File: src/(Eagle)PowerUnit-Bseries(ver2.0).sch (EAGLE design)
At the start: 292 parts, among them CON1 XT90PW-M, CON2 XT90PW-F, CON3 XT60PW-F, CON4 XT60PW-F, CON5 XT60PW-F, CON6 XT60PW-F, Q1 SQJA16EP-T1_GE3, Q10 SQJA16EP-T1_GE3, Q11 TMBT3906, Q12 TMBT3906, Q2 SSM3J332R, Q6 SQJA16EP-T1_GE3, SW1 SS-12SDP2, SW2 RDS-16S-1055-SMT-TR, SW3 SSSS213202, SW4 2MS1-T2-B4-M2-Q-E-S, SW5 2MS1-T2-B4-M2-Q-E-S, U1 LQFP64, U10 TC7S14F, U11 MCP6541T-I/LT, U12 MCP6541T-I/LT, U13 TC7S14F, U14 TCK420G, U15 TCKE805NAWSON10B_TOS-REC, U16 TC7SH00FULJ, U17 TC7S14F, U18 TC7S14F, U19 TC7SH00FULJ, U2 MCP2517FD, U20 TLP293, U21 TC7S14F, U22 TC7S14F, U23 TC7S14F, U24 MCP6541T-I/LT, U25 TC7S14F, U26 TC7SH00FULJ, U3 CH340E, U4 CZ-3A04, U5 AP63205WU-7, U6 CZ-3A04, U7 MCP6541T-I/LT, U8 CZ-3A04, U9 CZ-3A04, X1 XRCGB40M000F4M01R0, X2 RH100-24.000-18-1020-EXT-TR, X3 32.768K12.5PI/MC306

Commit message: develop_v2
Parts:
- removed R124: 10, CR0603:CR0603
- removed ZD2: MMBZ5248B-TP, MMBZ5248B-TP:MMBZ5248B-TP
- added LED10, LED9: SML-E12V8WT86, SML-E12V8WT86:SML-E12V8WT86
- added NTC1: NCU15WB473F60RC, NCU15WB473F60RC:NCU15WB473F60RC
- added R79: 680, CR0603:CR0603
- added R80: 33k, CR0603:CR0603
- added R81: 1.8k, CR0603:CR0603
- added R82: 100k, CR0603:CR0603
- added R83: 187k, CR0603:CR0603
- added R84: 0Ω, CR0603:CR0603
- added R85: 100, CR0603:CR0603
- added SB8: RSX101VAM-30TR, RSX101VAM-30TR:RSX101VAM-30TR
- added U27: MCP6541T-I/LT, MCP6541T-I:MCP6541T-I/LT
- R3: value 1 -> 10; device CR0603:CR0603 -> RSMF2JT10R0:RSMF2JT10R0
- R8, R9: value (none) -> 5.1k
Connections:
- removed net GND2: B1.3, C10.P$2, C11.P$2, C12.2, C13.P$1, C14.P$2, C15.P$2, C16.2, C17.2, C18.P$2, C19.P$2, C20.P$2, C21.P$2, C22.P$2, C23.P$2, C24.2, C25.P$2, C26.P$2, C27.1, C28.1, C29.1, C3.P$1, C30.1, C31.P$2, C32.P$2, C33.P$2, C34.P$2, C35.P$2, C36.P$2, C37.P$1, C38.P$1, C39.P$1, C4.R, C40.P$1, C41.P$1, C42.P$1, C43.P$1, C44.2, C45.2, C46.P$1, C47.P$2, C48.2, C49.2, C5.R, C50.P$2, C51.2, C52.2, C53.P$2, C54.2, C55.2, C56.P$2, C57.P$1, C58.P$1, C59.P$1, C60.P$1, C61.P$1, C62.P$1, C63.P$1, C64.P$1, C67.P$2, C68.2, C69.P$2, C7.CATHODE, C8.P$2, C9.2, D3.A, GND.1, JP2.1, JP3.1, JP4.1, JP5.1, JP7.1, LED4.C, LED5.C, LED6.C, LED7.C, ML1.11, ML1.5, ML1.7, POW.1, R100.LEFT, R102.LEFT, R105.LEFT, R107.LEFT, R11.RIGHT, R12.LEFT, R15.LEFT, R19.LEFT, R20.LEFT, R22.RIGHT, R29.LEFT, R30.LEFT, R31.LEFT, R37.LEFT, R38.LEFT, R41.LEFT, R45.RIGHT, R49.LEFT, R54.LEFT, R56.LEFT, R61.RIGHT, R66.RIGHT, R72.RIGHT, R75.LEFT, R76.LEFT, R8.LEFT, R9.LEFT, R95.LEFT, R97.LEFT, RJ45_1.2, RJ45_1.8, RJ45_1.LED2_K, RJ45_2.2, RJ45_2.8, RJ45_2.LED2_K, SB6.A, TLP1.CATHODE, TR1.E, TR2.E, U$1.VSS, U$4.GND, U1.P12, U1.P18, U1.P31, U1.P47, U1.P63, U10.GND, U11.VSS, U12.VSS, U13.GND, U15.GND, U2.VSS, U22.GND, U23.GND, U24.VSS, U25.GND, U26.GND, U3.GND, U4.VSS1, U4.VSS2, U5.GND, U6.VSS1, U6.VSS2, U7.VSS, U8.VSS1, U8.VSS2, U9.VSS1, U9.VSS2, USB1.GND, USB1.SHIELD, X2.SHIELD
- removed net N$112: Q1.G, Q6.G, R124.LEFT, ZD2.C
- new net N$120: LED9.A, R79.RIGHT
- new net N$121: R84.RIGHT, U3.RTS#
- new net N$122: R80.RIGHT, R81.LEFT, R83.LEFT, U27.IN+
- new net N$123: R84.LEFT, U3.CTS#
- new net N$124: LED10.A, R85.RIGHT
- new net N$126: R83.RIGHT, R85.LEFT, SB8.A, U27.OUT
- new net PGND: C1.CATHODE, C2.P$2, C65.P$2, C66.P$2, C70.P$2, C71.P$2, CON1.-, CON2.-, EDGE1.P28, EDGE1.P29, EDGE1.P30, EDGE1.P31, EDGE1.P32, EDGE1.P33, EDGE1.P34, EDGE1.P35, EDGE1.P36, EDGE1.P37, EDGE1.P38, EDGE1.P39, EDGE2.P28, EDGE2.P29, EDGE2.P30, EDGE2.P31, EDGE2.P32, EDGE2.P33, EDGE2.P34, EDGE2.P35, EDGE2.P36, EDGE2.P37, EDGE2.P38, EDGE2.P39, EDGE3.P28, EDGE3.P29, EDGE3.P30, EDGE3.P31, EDGE3.P32, EDGE3.P33, EDGE3.P34, EDGE3.P35, EDGE3.P36, EDGE3.P37, EDGE3.P38, EDGE3.P39, EDGE4.P28, EDGE4.P29, EDGE4.P30, EDGE4.P31, EDGE4.P32, EDGE4.P33, EDGE4.P34, EDGE4.P35, EDGE4.P36, EDGE4.P37, EDGE4.P38, EDGE4.P39, GND.2, H1.P$1, H2.P$1, H3.P$1, H4.P$1, INV_SW2.2, LED1.C, LED2.C, LED9.C, Q10.S, R119.LEFT, SW5.O, TLP1.GND, TLP3.CATHODE, TLP3.GND, U14.GND, U16.GND, U17.GND, U18.GND, U19.GND, U20.EMITTER, U21.GND, ZD1.A, ZD5.A
- new net SGND: B1.3, C10.P$2, C11.P$2, C12.2, C13.P$1, C14.P$2, C15.P$2, C16.2, C17.2, C18.P$2, C19.P$2, C20.P$2, C21.P$2, C22.P$2, C23.P$2, C24.2, C25.P$2, C26.P$2, C27.1, C28.1, C29.1, C3.P$1, C30.1, C31.P$2, C32.P$2, C33.P$2, C34.P$2, C35.P$2, C36.P$2, C37.P$1, C38.P$1, C39.P$1, C4.R, C40.P$1, C41.P$1, C42.P$1, C43.P$1, C44.2, C45.2, C46.P$1, C47.P$2, C48.2, C49.2, C5.R, C50.P$2, C51.2, C52.2, C53.P$2, C54.2, C55.2, C56.P$2, C57.P$1, C58.P$1, C59.P$1, C60.P$1, C61.P$1, C62.P$1, C63.P$1, C64.P$1, C67.P$2, C68.2, C69.P$2, C7.CATHODE, C8.P$2, C9.2, D3.A, GND.1, JP2.1, JP3.1, JP4.1, JP5.1, JP7.1, LED10.C, LED4.C, LED5.C, LED6.C, LED7.C, ML1.11, ML1.5, ML1.7, NTC1.1, POW.1, R100.LEFT, R102.LEFT, R105.LEFT, R107.LEFT, R11.RIGHT, R12.LEFT, R15.LEFT, R19.LEFT, R20.LEFT, R22.RIGHT, R29.LEFT, R30.LEFT, R31.LEFT, R37.LEFT, R38.LEFT, R41.LEFT, R45.RIGHT, R49.LEFT, R54.LEFT, R56.LEFT, R61.RIGHT, R66.RIGHT, R72.RIGHT, R75.LEFT, R76.LEFT, R8.LEFT, R81.RIGHT, R9.LEFT, R95.LEFT, R97.LEFT, RJ45_1.2, RJ45_1.8, RJ45_1.LED2_K, RJ45_2.2, RJ45_2.8, RJ45_2.LED2_K, SB6.A, TLP1.CATHODE, TR1.E, TR2.E, U$1.VSS, U$4.GND, U1.P12, U1.P18, U1.P31, U1.P47, U1.P63, U10.GND, U11.VSS, U12.VSS, U13.GND, U15.GND, U2.VSS, U22.GND, U23.GND, U24.VSS, U25.GND, U26.GND, U27.VSS, U3.GND, U4.VSS1, U4.VSS2, U5.GND, U6.VSS1, U6.VSS2, U7.VSS, U8.VSS1, U8.VSS2, U9.VSS1, U9.VSS2, USB1.GND, USB1.SHIELD, X2.SHIELD
- new net THERMAL: NTC1.2, R82.RIGHT, U1.P21, U27.IN-
- net +3V3: now also R80.LEFT, R82.LEFT, U27.VDD
- net CS1_OCD1: no longer C48.1, C51.1, C54.1, JP1.3, JP10.3, JP9.3, R24.LEFT, R63.LEFT, R69.LEFT
- net CS1_OCD2: no longer C49.1, C52.1, C55.1, JP1.1, JP10.1, JP9.1, R33.LEFT, R64.LEFT, R70.LEFT
- net CS2_OCD1: now also C48.1, JP1.3, R24.LEFT
- net CS2_OCD2: now also C49.1, JP1.1, R33.LEFT
- net CS3_OCD1: now also C51.1, JP9.3, R63.LEFT
- net CS3_OCD2: now also C52.1, JP9.1, R64.LEFT
- net CS4_OCD1: now also C54.1, JP10.3, R69.LEFT
- net CS4_OCD2: now also C55.1, JP10.1, R70.LEFT
- net GND: no longer C1.CATHODE, C2.P$2, C65.P$2, C66.P$2, C70.P$2, C71.P$2, CON1.-, CON2.-, EDGE1.P28, EDGE1.P29, EDGE1.P30, EDGE1.P31, EDGE1.P32, EDGE1.P33, EDGE1.P34, EDGE1.P35, EDGE1.P36, EDGE1.P37, EDGE1.P38, EDGE1.P39, EDGE2.P28, EDGE2.P29, EDGE2.P30, EDGE2.P31, EDGE2.P32, EDGE2.P33, EDGE2.P34, EDGE2.P35, EDGE2.P36, EDGE2.P37, EDGE2.P38, EDGE2.P39, EDGE3.P28, EDGE3.P29, EDGE3.P30, EDGE3.P31, EDGE3.P32, EDGE3.P33, EDGE3.P34, EDGE3.P35, EDGE3.P36, EDGE3.P37, EDGE3.P38, EDGE3.P39, EDGE4.P28, EDGE4.P29, EDGE4.P30, EDGE4.P31, EDGE4.P32, EDGE4.P33, EDGE4.P34, EDGE4.P35, EDGE4.P36, EDGE4.P37, EDGE4.P38, EDGE4.P39, GND.2, H1.P$1, H2.P$1, H3.P$1, H4.P$1, INV_SW2.2, LED1.C, LED2.C, Q10.S, R119.LEFT, SW5.O, TLP1.GND, TLP3.CATHODE, TLP3.GND, U14.GND, U16.GND, U17.GND, U18.GND, U19.GND, U20.EMITTER, U21.GND, ZD1.A, ZD5.A
- net N$11: now also R3.1; no longer R3.RIGHT
- net N$111: now also R3.2; no longer R3.LEFT, ZD2.A
- net N$25: now also C1.ANODE, R79.LEFT
- net N$26: now also Q1.G, Q6.G; no longer R124.RIGHT
- net SHUTDOWN: now also SB8.C
- net VCC: no longer C1.ANODE
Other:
- note added: "A"
- note added: "Default:closed"
- note added: "Default:open"
- note added: "Hysteresis:5℃(approximately)"
- note added: "Near the high-side MOSFETs"
- note added: "OTP"
- note added: "S=GND->normal mode S=VIN->silent mode"
- note removed: "Sピン=GND->通常モード Sピン=VIN->サイレントモード"
- moved on the sheet: B1, C1, C26, C67, C9, CON1, CON2, D3, FUSE1, LED1, R2

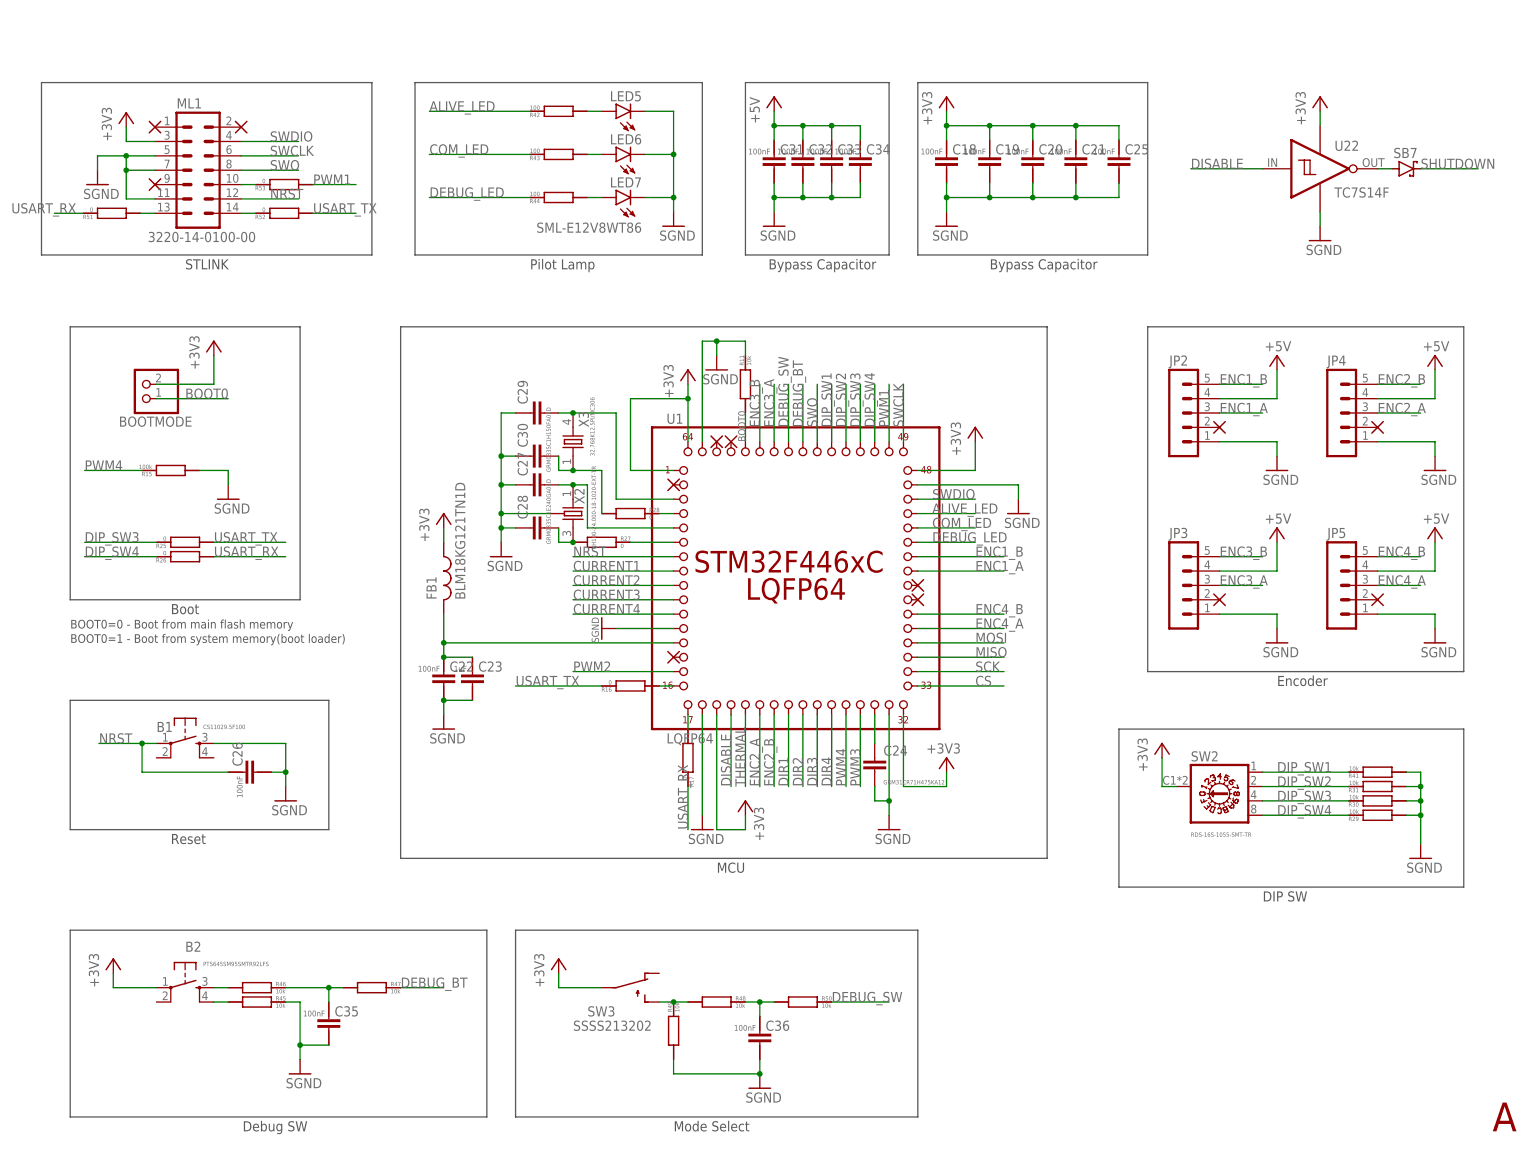
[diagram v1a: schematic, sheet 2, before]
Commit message: 2023/03/07 信号ラインの配線途中
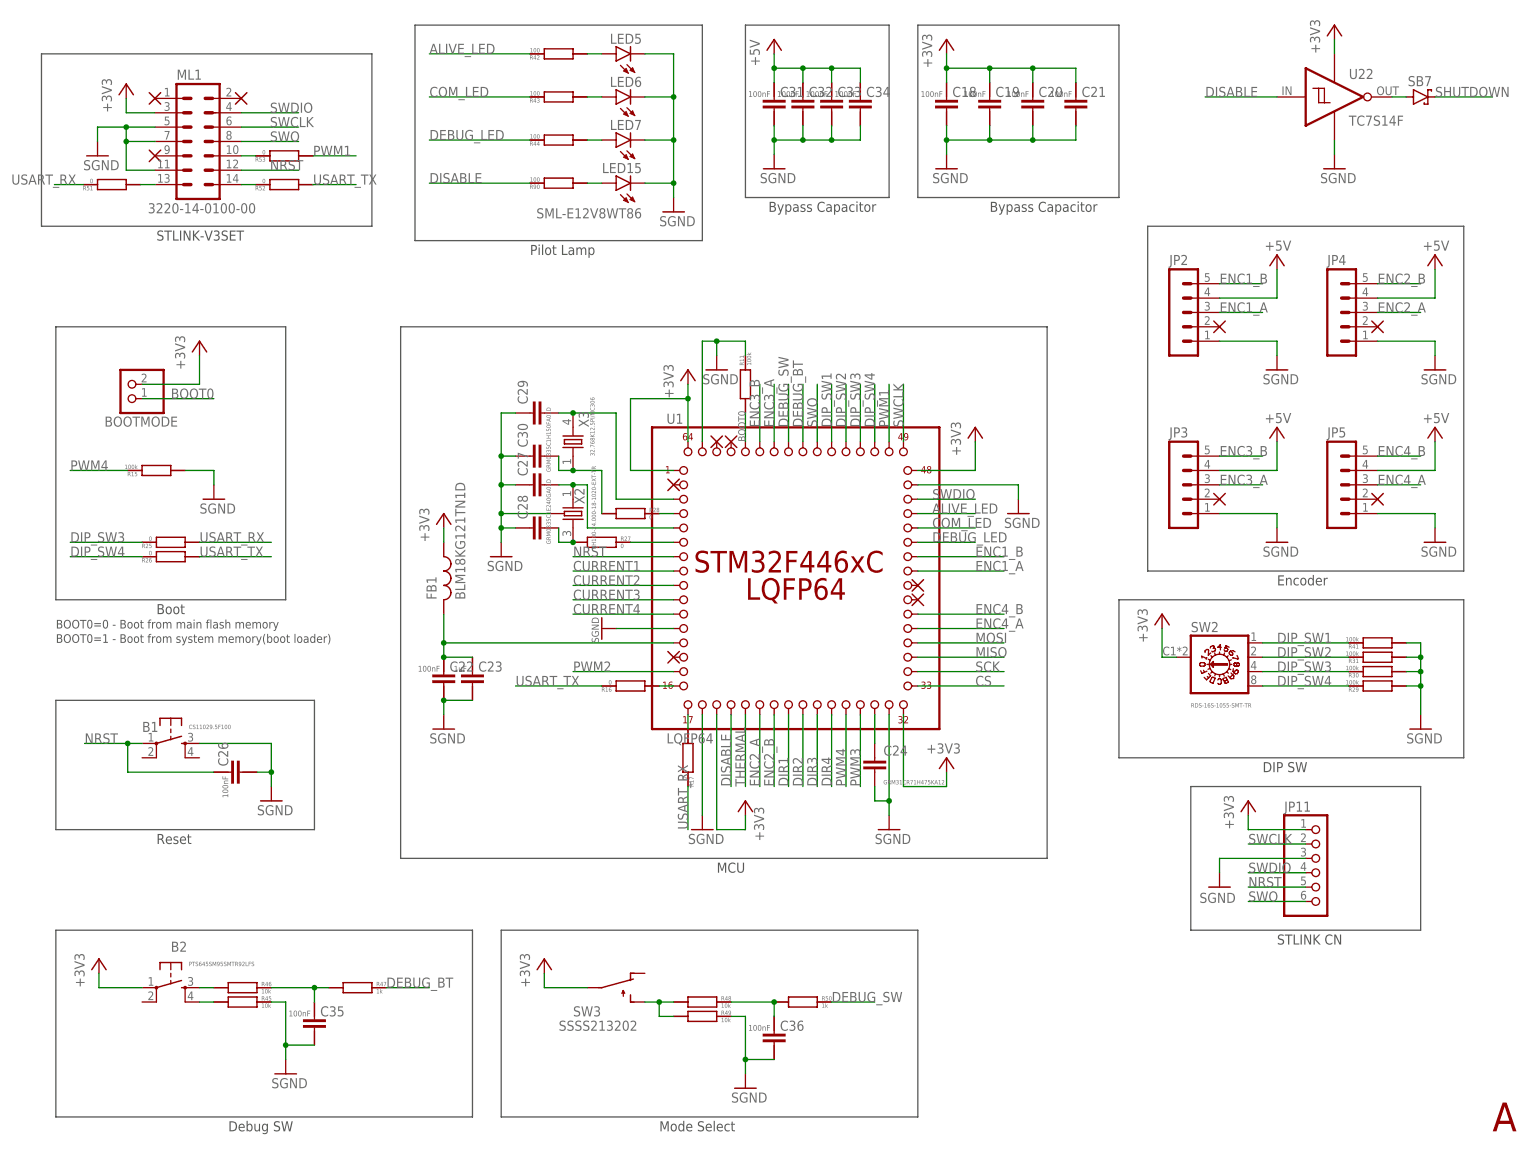
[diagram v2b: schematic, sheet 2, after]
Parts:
- removed C1: 50SEV470M16X16.5, 50SEV470M16X16.5:50SEV470M16X16.5
- removed C25: GCM188L81H104KA57, GCM188L81H104K57(0.1uF):GCM188L81H104KA57
- removed CON6: XT60PW-F, amass:XT60PW-F
- added C72, C73: GCM188L81H104KA57, GCM188L81H104K57(0.1uF):GCM188L81H104KA57
- added D4: GS2M-LTP, GS2M-LTP:GS2M-LTP
- added HEATSINK1: V2020B, V2020B:V2020B
- added IN: XT90PW-M, amass:XT90PW-M
- added JP11: (no value), pinhead:PINHD-1X6
- added LED11, LED12, LED13, LED14, LED15: SML-E12V8WT86, SML-E12V8WT86:SML-E12V8WT86
- added R86, R87, R89: 150, CR0603:CR0603
- added R88, R90: 100, CR0603:CR0603
- C39, C40, C41, C42, C58, C59, C62, C63: value GCM188L81H104KA57 -> GRM1885C1H102JA01D; device GCM188L81H104K57(0.1uF):GCM188L81H104KA57 -> GRM1885C1H102JA01D:GRM1885C1H102JA01D
- CON1: value XT90PW-M -> XT60PW-F; device amass:XT90PW-M -> amass:XT60PW-F
- CON2: value XT90PW-F -> XT60PW-F; device amass:XT90PW-F -> amass:XT60PW-F
- CON5: value XT60PW-F -> XT90PW-F; device amass:XT60PW-F -> amass:XT90PW-F
- D1, D2: value GS1010FL -> GS2M-LTP; device GS1010FL:GS1010FL -> GS2M-LTP:GS2M-LTP
- INV_SW1, INV_SW2: value (none) -> 02-JST; device pinhead:PINHD-1X2 -> con-jst-xh:02-JST
- R11, R29, R30, R31, R41: value 10k -> 100k
- R113, R116, R2, R5, R79: value 680 -> 1.1k
- R120: value 620 -> 1k
- R32: value 10k -> 10
- R4: value 220 -> 560
- R47, R50: value 10k -> 1k
- R76: value 36k -> 56k
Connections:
- removed net GND: EDGE1.P24, EDGE2.P24, EDGE3.P24, EDGE4.P24
- removed net N$15: CTRL1.2, CTRL2.2, R4.LEFT, THRU1.2, THRU2.2
- removed net VCC2: EDGE1.P27, EDGE2.P27, EDGE3.P27, EDGE4.P27
- new net E5V: C7.ANODE, JP6.3, L1.R, R86.RIGHT, U5.FB
- new net N$112: D4.A, R32.LEFT
- new net N$125: LED11.A, R86.LEFT
- new net N$127: LED15.A, R90.LEFT
- new net N$129: LED13.A, R89.LEFT
- new net N$130: LED14.A, R88.LEFT
- net +3V3: now also C72.P$1, EDGE1.P27, EDGE2.P27, EDGE3.P27, EDGE4.P27, JP11.1, R88.RIGHT; no longer C25.P$1
- net +5V: now also R89.RIGHT; no longer R32.RIGHT
- net 5V1: now also C73.P$1
- net CS1_REF1: now also C41.1; no longer C41.P$2
- net CS1_REF2: now also C42.1; no longer C42.P$2
- net CS2_REF1: now also C39.1; no longer C39.P$2
- net CS2_REF2: now also C40.1; no longer C40.P$2
- net CS3_REF1: now also C58.1; no longer C58.P$2
- net CS3_REF2: now also C59.1; no longer C59.P$2
- net CS4_REF1: now also C62.1; no longer C62.P$2
- net CS4_REF2: now also C63.1; no longer C63.P$2
- net DISABLE: now also R90.RIGHT
- net IP1: now also CON1.-; no longer CON3.-
- net IP2: now also CON2.-; no longer CON4.-
- net IP3: now also CON3.-; no longer CON5.-
- net IP4: now also CON4.-; no longer CON6.-
- net N$10: now also CON4.+; no longer CON6.+
- net N$103: no longer R32.LEFT
- net N$25: now also IN.+; no longer C1.ANODE, CON1.+
- net N$4: now also CON1.+; no longer CON3.+
- net N$5: now also CON2.+; no longer CON4.+
- net N$55: now also LED12.A, R87.LEFT; no longer C7.ANODE, JP6.3, L1.R, U5.FB
- net N$6: now also CON3.+; no longer CON5.+
- net N$63: now also R49.LEFT; no longer R49.RIGHT
- net N$95: now also D4.C
- net N$96: now also R32.RIGHT
- net NRST: now also JP11.5
- net PGND: now also C73.P$2, CON5.-, IN.-; no longer C1.CATHODE, CON1.-, CON2.-
- net SGND: now also C39.2, C40.2, C41.2, C42.2, C58.2, C59.2, C62.2, C63.2, C72.P$2, EDGE1.P24, EDGE2.P24, EDGE3.P24, EDGE4.P24, JP11.3, LED11.C, LED12.C, LED13.C, LED14.C, LED15.C, R49.RIGHT; no longer C25.P$2, C39.P$1, C40.P$1, C41.P$1, C42.P$1, C58.P$1, C59.P$1, C62.P$1, C63.P$1, R49.LEFT
- net SWCLK: now also JP11.2
- net SWDIO: now also JP11.4
- net SWO: now also JP11.6
- net U5V: now also R87.RIGHT
- net USART_RX: now also R25.LEFT; no longer R26.LEFT
- net USART_TX: now also R26.LEFT; no longer R25.LEFT
- net VCC: now also CON5.+, CTRL1.2, CTRL2.2, R4.LEFT, THRU1.2, THRU2.2; no longer CON2.+
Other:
- note added: "23.368℃/W"
- note added: "BOOT1"
- note added: "Continuous Max:92[A]"
- note added: "DeadTime:0.606ms(approximately)"
- note added: "RJ45(CH1)"
- note added: "RJ45(CH2)"
- note added: "STLINK CN"
- note added: "STLINK-V3SET"
- note added: "UVLO:5.434V"
- note added: "V_ON:5.883V"
- note added: "limit:1.35A"
- note added: "limit:1.948A"
- note removed: "DeadTime:0.568ms(approximately)"
- note removed: "RJ45"
- note removed: "STLINK"
- note removed: "limit:2.956A"
- moved on the sheet: B1, B2, BOOTMODE, C18, C19, C20, C21, C26, C31, C32, C33, C34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

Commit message: 2023/03/10の進捗
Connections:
- removed net CANH: R7.RIGHT, RJ45_1.3, RJ45_1.4, RJ45_2.3, RJ45_2.4, U$1.CANH
- removed net CANL: RJ45_1.5, RJ45_1.6, RJ45_2.5, RJ45_2.6, SW1.C, U$1.CANL
- new net CAN_H: R7.RIGHT, RJ45_1.5, RJ45_1.6, RJ45_2.5, RJ45_2.6, U$1.CANH
- new net CAN_L: RJ45_1.3, RJ45_1.4, RJ45_2.3, RJ45_2.4, SW1.C, U$1.CANL
- net PGND: no longer H3.P$1, H4.P$1
- net SGND: now also H3.P$1, H4.P$1
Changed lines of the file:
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@@
 <part name="CON5" library="amass" library_urn="urn:adsk.eagle:library:38637493" deviceset="XT90" device="PW-F" package3d_urn="urn:adsk.eagle:package:38637515/3"/>
 <part name="P+25" library="supply1" library_urn="urn:adsk.eagle:library:371" deviceset="VCC" device=""/>
+<part name="GND72" library="supply1" library_urn="urn:adsk.eagle:library:371" deviceset="GND" device=""/>
 </parts>
 <sheets>
@@
 <attribute name="VALUE" x="24.892" y="15.3162" size="1.778" layer="96"/>
 </instance>
-<instance part="SUPPLY4" gate="GND" x="12.7" y="15.24" smashed="yes"/>
+<instance part="SUPPLY4" gate="GND" x="7.62" y="25.4" smashed="yes"/>
 <instance part="USB1" gate="G$1" x="83.82" y="30.48" smashed="yes">
 <attribute name="VALUE" x="73.314" y="64.51" size="2" layer="96"/>
@@
 <attribute name="VALUE" x="66.04" y="297.18" size="1.778" layer="96" rot="R90"/>
 </instance>
+<instance part="GND72" gate="1" x="7.62" y="15.24" smashed="yes"/>
 </instances>
 <busses>
@@
 <pinref part="SUPPLY4" gate="GND" pin="GND"/>
 <pinref part="H1" gate="G$1" pin="P$1"/>
-<wire x1="12.7" y1="17.78" x2="12.7" y2="22.86" width="0.1524" layer="91"/>
-<wire x1="12.7" y1="22.86" x2="12.7" y2="27.94" width="0.1524" layer="91"/>
+<wire x1="7.62" y1="27.94" x2="12.7" y2="27.94" width="0.1524" layer="91"/>
 <wire x1="12.7" y1="27.94" x2="12.7" y2="33.02" width="0.1524" layer="91"/>
 <wire x1="12.7" y1="33.02" x2="22.86" y2="33.02" width="0.1524" layer="91"/>
@@
 <wire x1="22.86" y1="27.94" x2="12.7" y2="27.94" width="0.1524" layer="91"/>
 <junction x="12.7" y="27.94"/>
-<pinref part="H3" gate="G$1" pin="P$1"/>
-<wire x1="22.86" y1="22.86" x2="12.7" y2="22.86" width="0.1524" layer="91"/>
-<junction x="12.7" y="22.86"/>
-<pinref part="H4" gate="G$1" pin="P$1"/>
-<wire x1="22.86" y1="17.78" x2="12.7" y2="17.78" width="0.1524" layer="91"/>
-<junction x="12.7" y="17.78"/>
-<label x="9.652" y="11.176" size="1.778" layer="95"/>
+<label x="4.572" y="21.844" size="1.778" layer="95"/>
 </segment>
 <segment>
@@
 <label x="160.02" y="388.62" size="1.778" layer="95"/>
 </segment>
+<segment>
+<pinref part="H4" gate="G$1" pin="P$1"/>
+<pinref part="GND72" gate="1" pin="GND"/>
+<wire x1="22.86" y1="17.78" x2="12.7" y2="17.78" width="0.1524" layer="91"/>
+<pinref part="H3" gate="G$1" pin="P$1"/>
+<wire x1="12.7" y1="17.78" x2="7.62" y2="17.78" width="0.1524" layer="91"/>
+<wire x1="22.86" y1="22.86" x2="12.7" y2="22.86" width="0.1524" layer="91"/>
+<wire x1="12.7" y1="22.86" x2="12.7" y2="17.78" width="0.1524" layer="91"/>
+<junction x="12.7" y="17.78"/>
+<label x="4.572" y="12.7" size="1.778" layer="95"/>
+</segment>
 </net>
 <net name="THERMAL" class="0">
@@
 </busses>
 <nets>
-<net name="CANH" class="0">
+<net name="CAN_H" class="0">
 <segment>
 <pinref part="U$1" gate="G$1" pin="CANH"/>
@@
 </segment>
 <segment>
-<pinref part="RJ45_1" gate="G$1" pin="4"/>
-<wire x1="81.28" y1="116.84" x2="81.28" y2="109.22" width="0.1524" layer="91"/>
-<label x="81.28" y="109.22" size="1.778" layer="95" rot="R90"/>
+<pinref part="RJ45_1" gate="G$1" pin="5"/>
+<wire x1="83.82" y1="116.84" x2="83.82" y2="109.22" width="0.1524" layer="91"/>
+<label x="83.82" y="109.22" size="1.778" layer="95" rot="R90"/>
 </segment>
 <segment>
-<pinref part="RJ45_1" gate="G$1" pin="3"/>
-<wire x1="78.74" y1="116.84" x2="78.74" y2="109.22" width="0.1524" layer="91"/>
-<label x="78.74" y="109.22" size="1.778" layer="95" rot="R90"/>
+<pinref part="RJ45_1" gate="G$1" pin="6"/>
+<wire x1="86.36" y1="116.84" x2="86.36" y2="109.22" width="0.1524" layer="91"/>
+<label x="86.36" y="109.22" size="1.778" layer="95" rot="R90"/>
 </segment>
 <segment>
-<pinref part="RJ45_2" gate="G$1" pin="3"/>
-<wire x1="198.12" y1="116.84" x2="198.12" y2="109.22" width="0.1524" layer="91"/>
-<label x="198.12" y="109.22" size="1.778" layer="95" rot="R90"/>
+<pinref part="RJ45_2" gate="G$1" pin="5"/>
+<wire x1="203.2" y1="116.84" x2="203.2" y2="109.22" width="0.1524" layer="91"/>
+<label x="203.2" y="109.22" size="1.778" layer="95" rot="R90"/>
 </segment>
 <segment>
-<pinref part="RJ45_2" gate="G$1" pin="4"/>
-<wire x1="200.66" y1="116.84" x2="200.66" y2="109.22" width="0.1524" layer="91"/>
-<label x="200.66" y="109.22" size="1.778" layer="95" rot="R90"/>
+<pinref part="RJ45_2" gate="G$1" pin="6"/>
+<wire x1="205.74" y1="116.84" x2="205.74" y2="109.22" width="0.1524" layer="91"/>
+<label x="205.74" y="109.22" size="1.778" layer="95" rot="R90"/>
 </segment>
 </net>
-<net name="CANL" class="0">
+<net name="CAN_L" class="0">
 <segment>
 <pinref part="U$1" gate="G$1" pin="CANL"/>
@@
 </segment>
 <segment>
-<pinref part="RJ45_1" gate="G$1" pin="5"/>
-<wire x1="83.82" y1="116.84" x2="83.82" y2="109.22" width="0.1524" layer="91"/>
-<label x="83.82" y="109.22" size="1.778" layer="95" rot="R90"/>
+<pinref part="RJ45_1" gate="G$1" pin="3"/>
+<wire x1="78.74" y1="116.84" x2="78.74" y2="109.22" width="0.1524" layer="91"/>
+<label x="78.74" y="109.22" size="1.778" layer="95" rot="R90"/>
 </segment>
 <segment>
-<pinref part="RJ45_1" gate="G$1" pin="6"/>
-<wire x1="86.36" y1="116.84" x2="86.36" y2="109.22" width="0.1524" layer="91"/>
-<label x="86.36" y="109.22" size="1.778" layer="95" rot="R90"/>
+<pinref part="RJ45_1" gate="G$1" pin="4"/>
+<wire x1="81.28" y1="116.84" x2="81.28" y2="109.22" width="0.1524" layer="91"/>
+<label x="81.28" y="109.22" size="1.778" layer="95" rot="R90"/>
 </segment>
 <segment>
-<pinref part="RJ45_2" gate="G$1" pin="5"/>
-<wire x1="203.2" y1="116.84" x2="203.2" y2="109.22" width="0.1524" layer="91"/>
-<label x="203.2" y="109.22" size="1.778" layer="95" rot="R90"/>
+<pinref part="RJ45_2" gate="G$1" pin="3"/>
+<wire x1="198.12" y1="116.84" x2="198.12" y2="109.22" width="0.1524" layer="91"/>
+<label x="198.12" y="109.22" size="1.778" layer="95" rot="R90"/>
 </segment>
 <segment>
-<pinref part="RJ45_2" gate="G$1" pin="6"/>
-<wire x1="205.74" y1="116.84" x2="205.74" y2="109.22" width="0.1524" layer="91"/>
-<label x="205.74" y="109.22" size="1.778" layer="95" rot="R90"/>
+<pinref part="RJ45_2" gate="G$1" pin="4"/>
+<wire x1="200.66" y1="116.84" x2="200.66" y2="109.22" width="0.1524" layer="91"/>
+<label x="200.66" y="109.22" size="1.778" layer="95" rot="R90"/>
 </segment>
 </net>

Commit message: 2023/03/20の進捗
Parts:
- removed HEATSINK1: V2020B, V2020B:V2020B
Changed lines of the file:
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@@
 <part name="R90" library="CR0603" deviceset="CR0603" device="" value="100"/>
 <part name="LED15" library="SML-E12V8WT86" deviceset="SML-E12V8WT86" device=""/>
-<part name="HEATSINK1" library="V2020B" deviceset="V2020B" device=""/>
 <part name="GND57" library="supply1" library_urn="urn:adsk.eagle:library:371" deviceset="GND" device=""/>
 <part name="C72" library="GCM188L81H104K57(0.1uF)" deviceset="GCM188L81H104KA57" device=""/>
@@
 <attribute name="NAME" x="334.772" y="67.056" size="0.762" layer="95" rot="R180"/>
 </instance>
-<instance part="HEATSINK1" gate="G$1" x="236.22" y="365.76" smashed="yes" rot="R270">
-<attribute name="NAME" x="231.14" y="367.411" size="1.778" layer="95"/>
-<attribute name="VALUE" x="233.68" y="362.077" size="1.778" layer="96"/>
-</instance>
 <instance part="GND57" gate="1" x="162.56" y="391.16" smashed="yes"/>
